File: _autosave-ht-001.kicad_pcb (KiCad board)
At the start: 2 copper layers, 40 x 25 mm, 30 parts, among them J1 USB_A, U1 CP2102N, U2 TPD3E001, U3 LP5912, U4 ICM20689, U5 MCP73831, U6 ESP32-WROOM, U7 BME680, U8 SPK0838HT4H-B

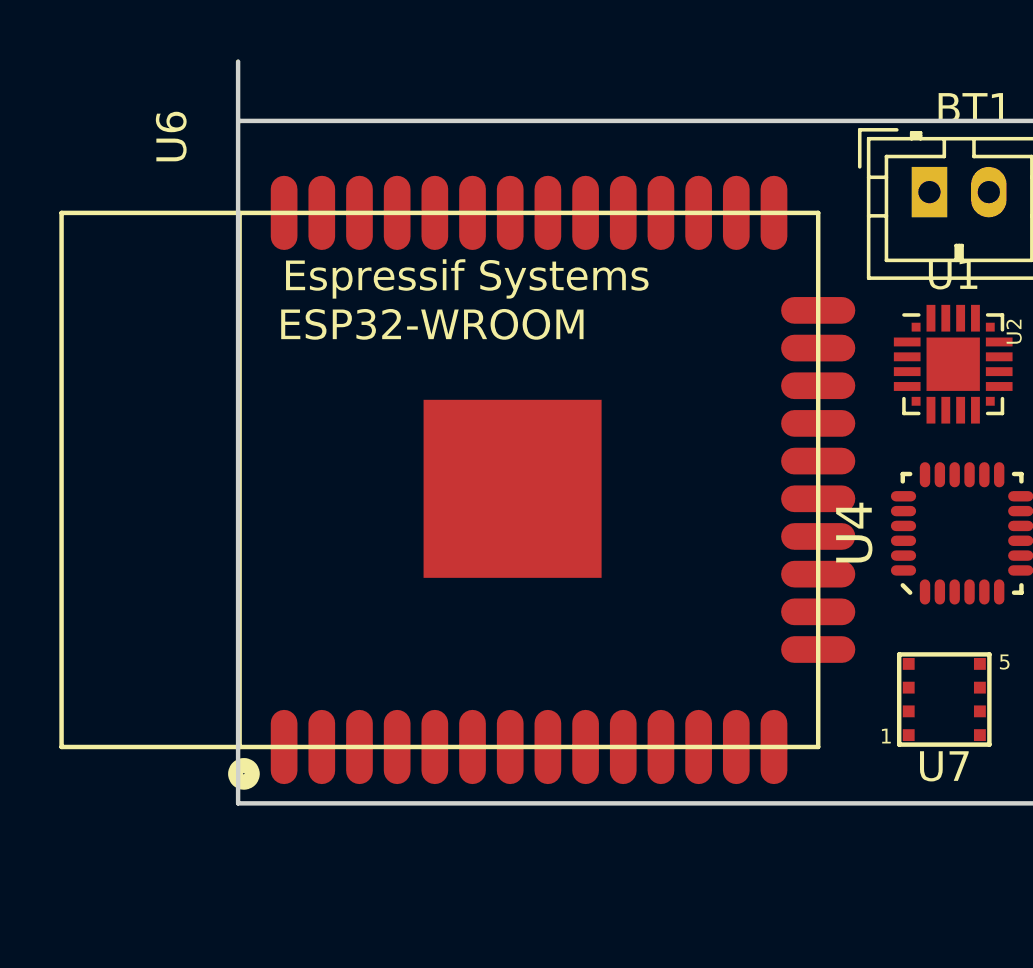
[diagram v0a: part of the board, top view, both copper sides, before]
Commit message: switch to single IC for gyro/accel
bit of schematic cleanup too
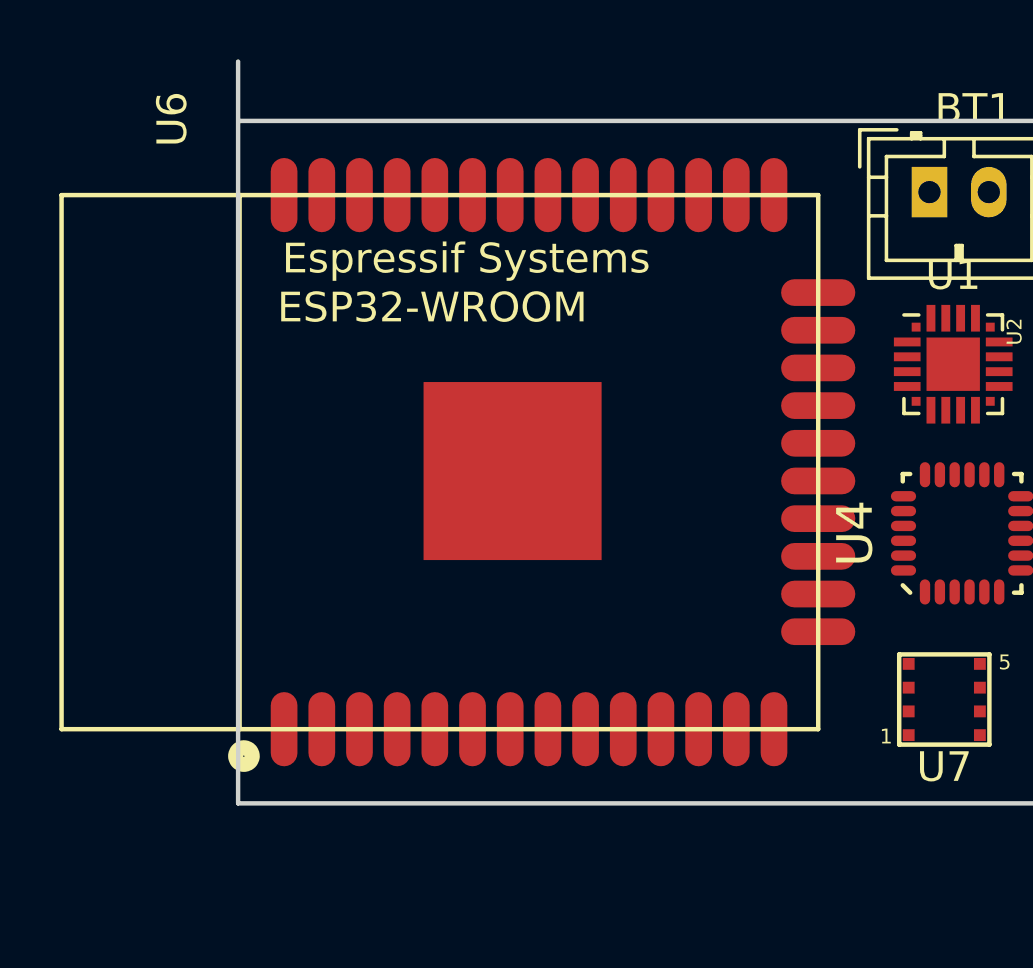
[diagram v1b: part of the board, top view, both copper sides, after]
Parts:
- moved U6 0.60 mm to (106.8, 113.5)
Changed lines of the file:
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@@
   )
   (module manfangfp:ESP32-WROOM (layer F.Cu)
-    (at 106.8 114.1 270)
+    (at 106.8 113.5 270)
     (fp_text reference U6 (at -11.557 9.017 270) (layer F.SilkS)
       (effects (font (size 1 1) (thickness 0.15)))

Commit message: "final" schematic cleanup
is joke
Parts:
- BT1: footprint Connectors_JST:JST_PH_B2B-PH-K_02x2.00mm_Straight -> Connectors_JST:JST_PH_B2B-PH-SM4-TB_02x2.00mm_Straight
- C1, C10, C11, C12, C13, C2, C3, C4, C5, C6, C7, C8, C9: footprint Capacitors_SMD:C_0201 -> Capacitors_SMD:C_0402
- R1, R2, R3, R4, R5, R6: footprint Resistors_SMD:R_0201 -> Resistors_SMD:R_0402
- moved R2 41.6 mm to (125.0, 101.4), turned to 90 degrees
- moved C1 40.5 mm to (127.3, 101.6), turned to 270 degrees
- moved D1 40.4 mm to (151.3, 108.2), turned to 90 degrees
- moved R3 40.2 mm to (123.1, 101.2), turned to 90 degrees
- moved C4 38.6 mm to (129.9, 100.2), turned to 180 degrees
- moved C6 36.7 mm to (129.9, 97.3), turned to 180 degrees
- moved R4 36.4 mm to (120.8, 121.4), turned to 270 degrees
- moved C9 34.8 mm to (129.9, 98.9)
- moved C13 34.1 mm to (135.2, 100.0), turned to 270 degrees
- moved C5 33.7 mm to (129.8, 96.1), turned to 180 degrees
- moved C12 33.4 mm to (150.6, 112.8), turned to 90 degrees
- moved C11 32.3 mm to (130.5, 113.5)
- moved R5 30.7 mm to (151.3, 110.6), turned to 90 degrees
- moved C3 30.6 mm to (130.4, 111.5), turned to 90 degrees
- moved C8 30.2 mm to (131.8, 110.2)
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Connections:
- C11 pad 1: Net-(BT1-Pad1) -> Net-(C11-Pad1)
- R5 pad 1: Net-(D1-Pad1) -> Net-(R5-Pad1)
- R5 pad 2: Net-(R5-Pad2) -> Net-(D1-Pad1)
- U5 pad 1: Net-(R5-Pad2) -> Net-(R5-Pad1)
- U5 pad 2: Net-(C1-Pad1) -> Net-(C11-Pad1)
- U6 pad 13: /MCLK -> (no net)
- U6 pad 14: /MDATA -> (no net)
- U6 pad 16: (no net) -> /AINT
- U6 pad 20: /AINT -> (no net)
- U6 pad 23: (no net) -> /MDATA
- U6 pad 24: (no net) -> /MCLK
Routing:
- net (no net): track 0.65 -> 0.00 mm
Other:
- board size 40 x 25 mm -> 45 x 22 mm
- net class Default: via_dia 0.6 -> 0.4
- net class Vdd added: clearance 0.1, trace_width 0.3, via_dia 0.4, via_drill 0.3

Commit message: cleanup changes
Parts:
- added C14: 0.1uF, Capacitors_SMD:C_0402, F.Cu at (127.9, 123.4)
- added R10: R, Resistors_SMD:R_0402, F.Cu at (122.4, 104.4)
- added R7: 0, Resistors_SMD:R_0402, F.Cu at (122.4, 108.6)
- added R8: 0, Resistors_SMD:R_0402, F.Cu at (122.4, 107.2)
- added R9: R, Resistors_SMD:R_0402, F.Cu at (122.4, 105.8)
- C1, C11: value 4.7uF -> 0.1uF
- C12: value 0.1uF -> 4.7uF
- C3: value 0.1uF -> 10nF
- C4: value 10nF -> 0.1uF
- C6: value 0.1uF -> 0.47uF
- C9: value 0.47uF -> 4.7uF
- R4: value 10k -> 470
- R5: value 470 -> 5.6k
- R6: value 5.6k -> 10k
- U1: value CP2102N -> BME680; footprint Housings_DFN_QFN:SiliconLabs_QFN-20-1EP_3x3mm_Pitch0.5mm -> manfangfp:BME680
- U2: value TPD3E001 -> ESP32-WROOM; footprint manfangfp:TPD3E001_USON_1.45mmx1mm -> manfangfp:ESP32-WROOM
- U3: value LP5912 -> TPD3E001; footprint manfangfp:WSON-6_2x2mm_Pitch0.65mm -> manfangfp:TPD3E001_USON_1.45mmx1mm
- U5: value MCP73831 -> LP5912; footprint manfangfp:SOT-23-5 -> manfangfp:WSON-6_2x2mm_Pitch0.65mm
- U6: value ESP32-WROOM -> MCP73831; footprint manfangfp:ESP32-WROOM -> manfangfp:SOT-23-5
- U7: value BME680 -> SPK0838HT4H-B; footprint manfangfp:BME680 -> manfangfp:SPK0838HT4H
- U8: value SPK0838HT4H-B -> CP2102N; footprint manfangfp:SPK0838HT4H -> Housings_DFN_QFN:SiliconLabs_QFN-20-1EP_3x3mm_Pitch0.5mm
- moved U2 29.8 mm to (106.8, 114.0), turned to 270 degrees
- moved U6 27.2 mm to (134.0, 113.2), turned to 90 degrees
- moved C1 21.9 mm to (125.2, 123.4), turned to 180 degrees
- moved R5 20.7 mm to (131.0, 114.4), turned to 270 degrees
- moved D1 20.4 mm to (131.0, 110.6), turned to 0 degrees
- moved C7 20.0 mm to (136.1, 118.6)
- moved C12 19.9 mm to (131.2, 108.2), turned to 270 degrees
- moved C5 19.8 mm to (122.0, 114.2), turned to 270 degrees
- moved R3 19.4 mm to (124.0, 120.6), turned to 270 degrees
- moved R2 19.4 mm to (122.3, 120.6), turned to 270 degrees
- moved C4 15.5 mm to (123.2, 114.2), turned to 270 degrees
- moved U1 15.5 mm to (127.0, 121.1)
- moved C6 14.8 mm to (126.0, 111.6)
- moved R4 13.7 mm to (131.0, 112.2)
- moved C9 12.5 mm to (134.1, 110.6), turned to 180 degrees
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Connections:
- BT1 pad 1: Net-(BT1-Pad1) -> +Vbat
- C1 pad 1: Net-(C1-Pad1) -> +3V3
- C10 pad 1: Net-(BT1-Pad1) -> +Vbat
- C11 pad 1: Net-(C11-Pad1) -> GND
- C11 pad 2: GND -> +3V3
- C12 pad 1: GND -> +Vusb
- C12 pad 2: +3V3 -> GND
- C13 pad 1: +3V3 -> +Vusb
- C2 pad 1: Net-(C1-Pad1) -> GND
- C2 pad 2: GND -> +Vusb
- C3 pad 1: GND -> +3V3
- C3 pad 2: Net-(C1-Pad1) -> GND
- C4 pad 1: GND -> +3V3
- C4 pad 2: +3V3 -> GND
- C5 pad 1: GND -> +3V3
- C5 pad 2: +3V3 -> GND
- C6 pad 1: GND -> Net-(C6-Pad1)
- C6 pad 2: +3V3 -> GND
- C7 pad 1: Net-(BT1-Pad1) -> +Vbat
- C9 pad 1: Net-(C9-Pad1) -> +Vusb
- D1 pad 2: Net-(C1-Pad1) -> +Vusb
- J1 pad 1: Net-(C1-Pad1) -> +Vusb
- J1 pad 2: Net-(J1-Pad2) -> /D-
- J1 pad 3: Net-(J1-Pad3) -> /D+
- R1 pad 1: Net-(C1-Pad1) -> +3V3
- R4 pad 1: +3V3 -> Net-(D1-Pad1)
- R5 pad 2: Net-(D1-Pad1) -> GND
- R6 pad 1: Net-(R6-Pad1) -> +Vusb
- R6 pad 2: GND -> Net-(R6-Pad2)
- U1 pad 1: (no net) -> GND
- U1 pad 2: (no net) -> +3V3
- U1 pad 3: GND -> /SDA
- U1 pad 4: Net-(J1-Pad3) -> /SCL
- U1 pad 5: Net-(J1-Pad2) -> GND
- U1 pad 6: Net-(C1-Pad1) -> +3V3
- U1 pad 7: Net-(C1-Pad1) -> GND
- U1 pad 8: Net-(C1-Pad1) -> +3V3
- U2 pad 1: Net-(J1-Pad2) -> GND
- U2 pad 2: Net-(J1-Pad3) -> +3V3
- U2 pad 3: GND -> +3V3
- U2 pad 6: Net-(C1-Pad1) -> (no net)
- U3 pad 1: +3V3 -> /D-
- U3 pad 2: (no net) -> /D+
- U3 pad 3: (no net) -> GND
- U3 pad 4: Net-(BT1-Pad1) -> (no net)
- U3 pad 5: GND -> (no net)
- U3 pad 6: Net-(BT1-Pad1) -> +Vusb
- U4 pad 10: Net-(C9-Pad1) -> Net-(C6-Pad1)
- U4 pad 22: Net-(R4-Pad2) -> Net-(R1-Pad2)
- U5 pad 1: Net-(R5-Pad1) -> +3V3
- U5 pad 2: Net-(C11-Pad1) -> (no net)
- U5 pad 3: Net-(BT1-Pad1) -> (no net)
- U5 pad 4: Net-(R6-Pad1) -> +Vbat
- U5 pad 5: (no net) -> GND
- U6 pad 1: GND -> Net-(R4-Pad2)
- U6 pad 2: +3V3 -> GND
- U6 pad 3: +3V3 -> +Vbat
- U6 pad 4: (no net) -> +Vusb
- U6 pad 5: (no net) -> Net-(R5-Pad1)
- U7 pad 1: GND -> +3V3
- U7 pad 2: +3V3 -> (no net)
- U7 pad 3: /SDA -> /MCLK
- U7 pad 4: /SCL -> /MDATA
- U7 pad 6: +3V3 -> GND
- U7 pad 8: +3V3 -> GND
- U8 pad 1: +3V3 -> (no net)
- U8 pad 3: /MCLK -> GND
- U8 pad 4: /MDATA -> /D+
- U8 pad 5: GND -> /D-
- U8 pad 6: GND -> +Vusb
- U8 pad 7: GND -> +Vusb
- U8 pad 8: GND -> +Vusb
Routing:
- net +3V3: track 0.00 -> 78.8 mm
- net GND: track 0.00 -> 43.4 mm, vias 0 -> 39
- net +Vusb: track 0.00 -> 23.9 mm
- net /MDATA: track 0.00 -> 22.0 mm
- net /RTS: track 0.00 -> 20.4 mm, vias 0 -> 2
- net /TXD: track 0.00 -> 18.8 mm
- net /D+: track 0.00 -> 18.4 mm, vias 0 -> 2
- net /SCL: track 0.00 -> 17.7 mm, vias 0 -> 3
- net /D-: track 0.00 -> 17.2 mm, vias 0 -> 2
- net /RXD: track 0.00 -> 16.9 mm
- net +Vbat: track 0.00 -> 16.5 mm
- net /SDA: track 0.00 -> 15.7 mm, vias 0 -> 2
- net /CTS: track 0.00 -> 15.7 mm
- net /MCLK: track 0.00 -> 15.3 mm
- net Net-(R4-Pad2): track 0.00 -> 7.21 mm
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- added copper zone on B.Cu, net GND
